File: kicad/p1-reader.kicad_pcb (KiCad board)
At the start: 2 copper layers, 63.9 x 24 mm, 11 parts, among them J1 RJ12, J2 ESP32 left, J3 ESP32 right, U1 4N35

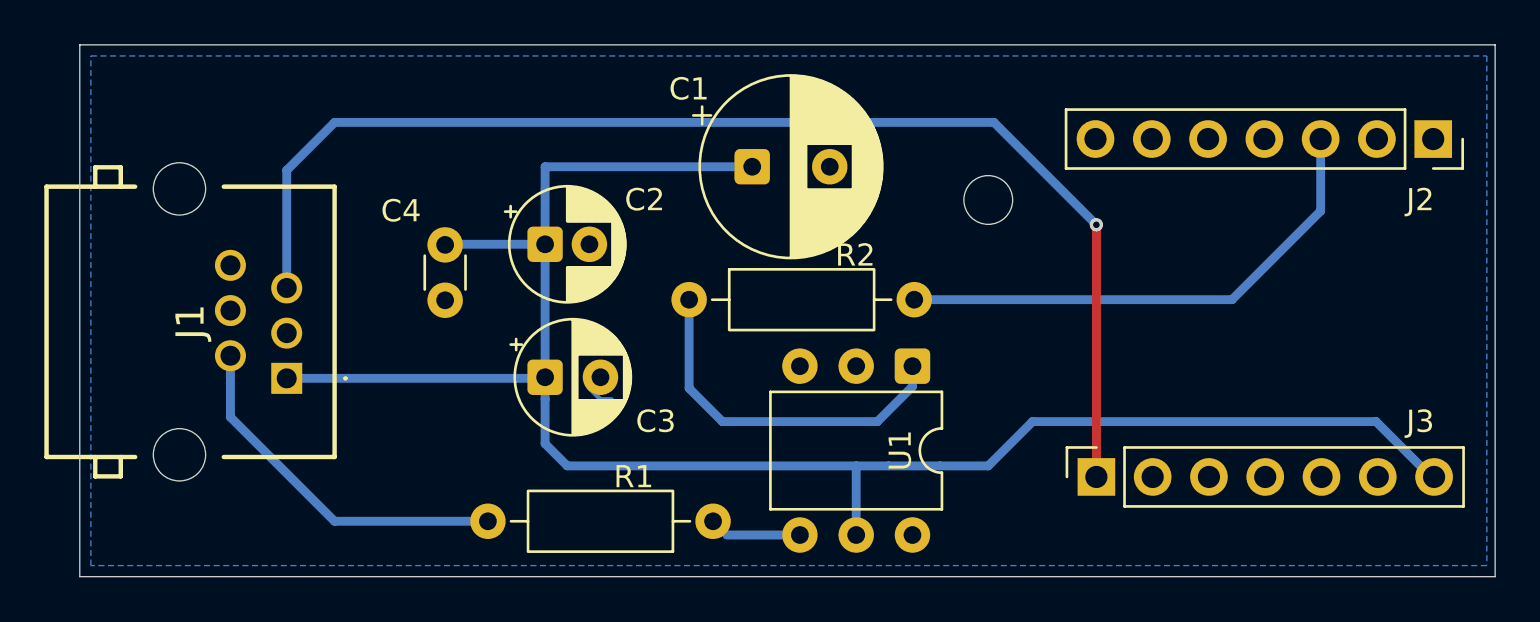
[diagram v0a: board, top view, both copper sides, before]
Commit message: Add status LED
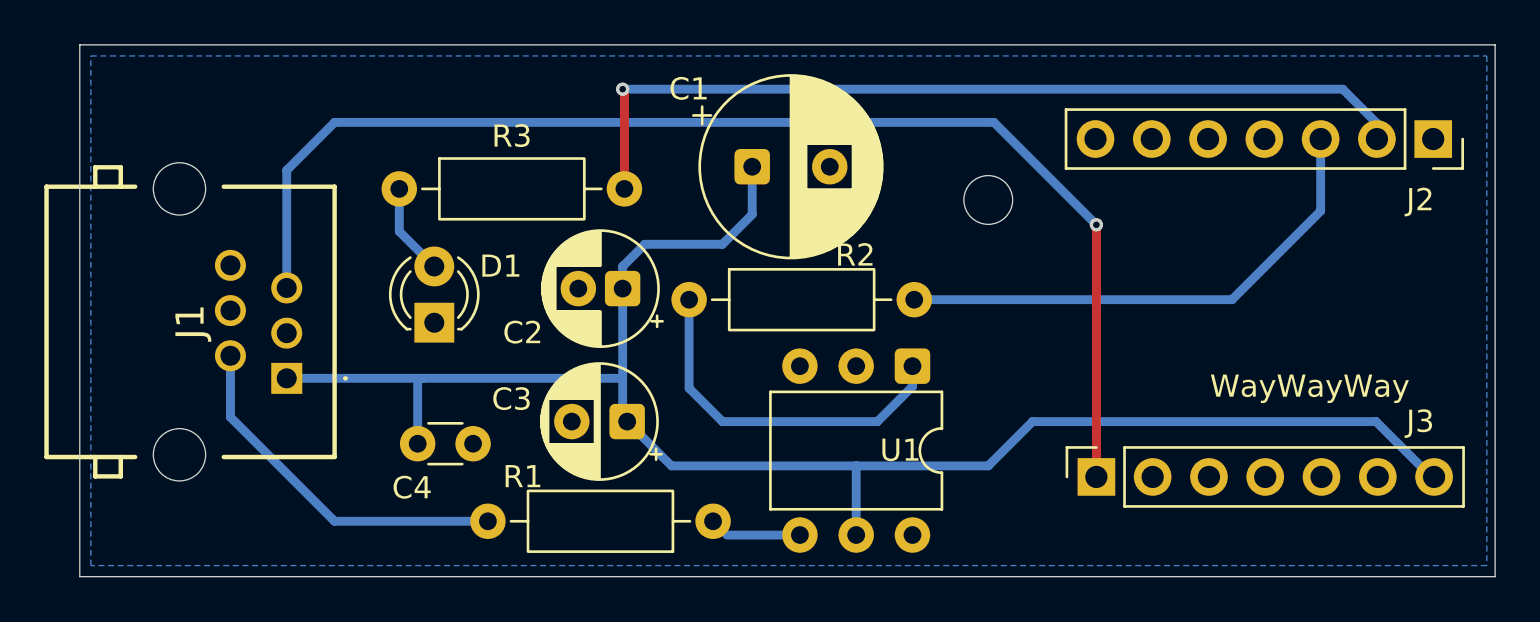
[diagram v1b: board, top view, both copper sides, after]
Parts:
- added D1: Status, LED_THT:LED_D3.0mm, F.Cu at (106.0, 89.0)
- added R3: 56, Resistor_THT:R_Axial_DIN0207_L6.3mm_D2.5mm_P10.16mm_Horizontal, F.Cu at (104.4, 83.0)
- moved C4 9.06 mm to (105.2, 94.5), turned to 0 degrees
- moved C3 4.21 mm to (114.7, 93.5), turned to 180 degrees
- moved C2 4.03 mm to (114.5, 87.5), turned to 180 degrees
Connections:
- J2 pad 2: unconnected-(J2-Pin_2-Pad2) -> Status_LED
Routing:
- net Status_LED: track 0.00 -> 39.9 mm, vias 0 -> 1
- net +5V: track 84.5 -> 76.5 mm
- net Net-(D1-A): track 0.00 -> 4.15 mm
- net Data_GND: track 1.21 -> 0.00 mm
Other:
- board text added: "WayWayWay"

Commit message: Update for Stoen
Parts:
- D1: value Status -> Status LED
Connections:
- J3 pad 5: unconnected-(J3-Pin_5-Pad5) -> +3V3
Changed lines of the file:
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@@
 	(net 11 "unconnected-(J2-Pin_5-Pad5)")
 	(net 12 "unconnected-(J3-Pin_4-Pad4)")
-	(net 13 "unconnected-(J3-Pin_5-Pad5)")
+	(net 13 "+3V3")
 	(net 14 "unconnected-(J3-Pin_3-Pad3)")
 	(net 15 "unconnected-(J3-Pin_2-Pad2)")
@@
 			)
 		)
-		(property "Value" "Status"
+		(property "Value" "Status LED"
 			(at -1.46 0 180)
 			(layer "F.Fab")
@@
 			(layers "*.Cu" "*.Mask")
 			(remove_unused_layers no)
-			(net 13 "unconnected-(J3-Pin_5-Pad5)")
+			(net 13 "+3V3")
 			(pinfunction "Pin_5")
-			(pintype "passive+no_connect")
+			(pintype "passive")
 		)
 		(pad "6" thru_hole circle
